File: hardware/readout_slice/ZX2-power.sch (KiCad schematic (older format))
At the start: 15 parts

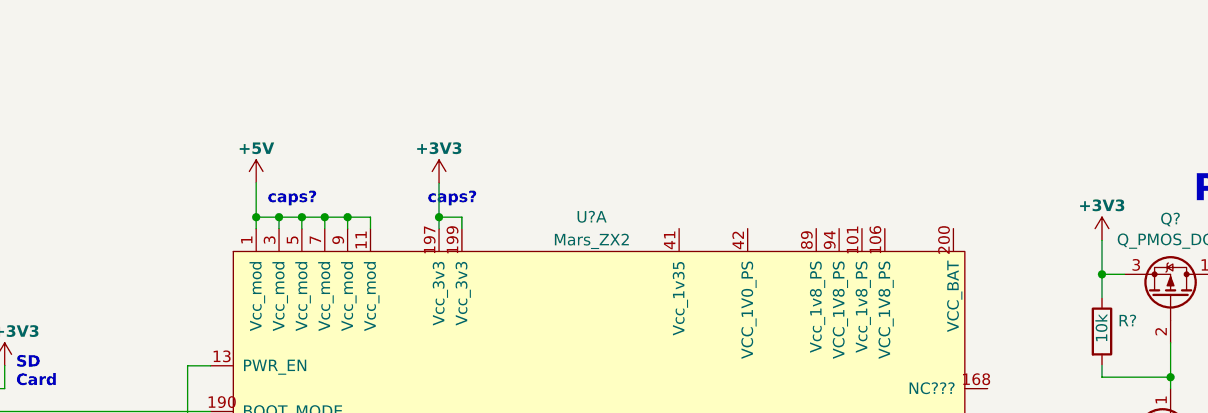
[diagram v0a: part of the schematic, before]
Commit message: more on readout_slice
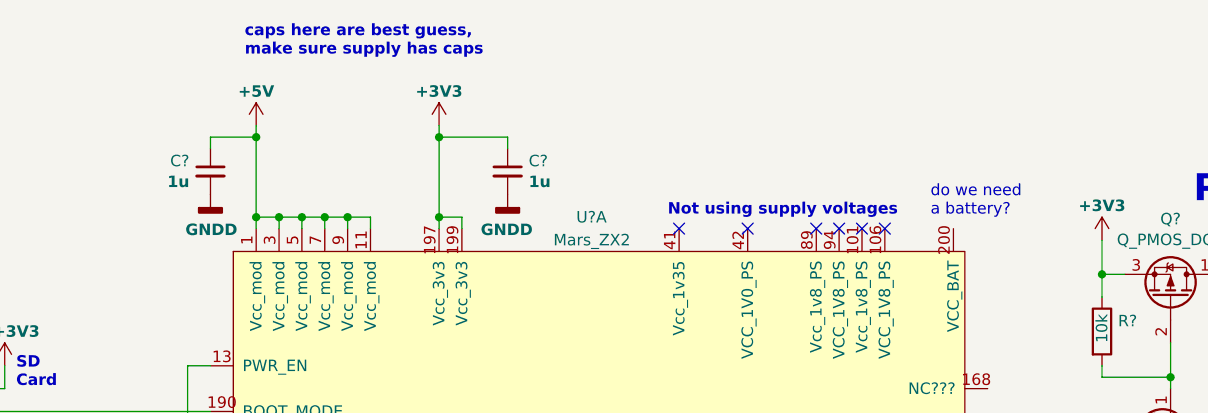
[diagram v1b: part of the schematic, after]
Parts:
- added C? (x2): 1u, symbol Device:C_Small
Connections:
- net +3V3: now also C?.1
- net +5V: now also C?.1
- net GNDD: now also C?.2, C?.2
- no-connect marks 0 -> 6
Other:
- note added: "Not using supply voltages"
- note added: "caps here are best guess,\nmake sure supply has caps"
- note added: "do we need\na battery?"
- note removed: "caps?"
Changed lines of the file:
@@
 $Descr A4 11693 8268
 encoding utf-8
-Sheet 7 10
+Sheet 5 10
 Title ""
 Date ""
@@
 Comment4 ""
 $EndDescr
-Text Notes 4350 2300 0    50   ~ 10
-caps?
-Wire Wire Line
-	4400 2350 4400 2200
+Wire Wire Line
+	4400 2350 4400 2000
 Connection ~ 4400 2350
 Wire Wire Line
@@
 	0    1    1    0
 $EndComp
-Text Notes 3650 2300 0    50   ~ 10
-caps?
 $Comp
 L power:+5V #PWR?
 U 1 1 60728782
-P 3600 2200
+P 3600 1950
 AR Path="/60728782" Ref="#PWR?"  Part="1"
 AR Path="/603D0C5A/60728782" Ref="#PWR?"  Part="1"
 AR Path="/6068976B/60728782" Ref="#PWR?"  Part="1"
 AR Path="/6086954E/608F2656/60728782" Ref="#PWR?"  Part="1"
-F 0 "#PWR?" H 3600 2050 50  0001 C CNN
-F 1 "+5V" H 3600 2350 50  0000 C CNB
-F 2 "" H 3600 2200 50  0001 C CNN
-F 3 "" H 3600 2200 50  0001 C CNN
-	1    3600 2200
+F 0 "#PWR?" H 3600 1800 50  0001 C CNN
+F 1 "+5V" H 3600 2100 50  0000 C CNB
+F 2 "" H 3600 1950 50  0001 C CNN
+F 3 "" H 3600 1950 50  0001 C CNN
+	1    3600 1950
 	1    0    0    -1
 $EndComp
@@
 L power:+3V3 #PWR?
 U 1 1 60728788
-P 4400 2200
+P 4400 1950
 AR Path="/60728788" Ref="#PWR?"  Part="1"
 AR Path="/603D0C5A/60728788" Ref="#PWR?"  Part="1"
 AR Path="/6068976B/60728788" Ref="#PWR?"  Part="1"
 AR Path="/6086954E/608F2656/60728788" Ref="#PWR?"  Part="1"
-F 0 "#PWR?" H 4400 2050 50  0001 C CNN
-F 1 "+3V3" H 4400 2350 50  0000 C CNB
-F 2 "" H 4400 2200 50  0001 C CNN
-F 3 "" H 4400 2200 50  0001 C CNN
-	1    4400 2200
+F 0 "#PWR?" H 4400 1800 50  0001 C CNN
+F 1 "+3V3" H 4400 2100 50  0000 C CNB
+F 2 "" H 4400 1950 50  0001 C CNN
+F 3 "" H 4400 1950 50  0001 C CNN
+	1    4400 1950
 	1    0    0    -1
 $EndComp
@@
 Wire Wire Line
 	3700 2400 3700 2350
-Wire Wire Line
-	3600 2350 3600 2200
 Connection ~ 3600 2350
 Wire Wire Line
@@
 Wire Notes Line width 39
 	4300 6300 4300 7850
+NoConn ~ 5450 2400
+NoConn ~ 5750 2400
+NoConn ~ 6050 2400
+NoConn ~ 6150 2400
+NoConn ~ 6250 2400
+NoConn ~ 6350 2400
+Text Notes 5400 2350 0    50   ~ 10
+Not using supply voltages
+Text Notes 6550 2350 0    50   ~ 0
+do we need\na battery?
+$Comp
+L Device:C_Small C?
+U 1 1 611B7B1F
+P 3400 2150
+F 0 "C?" H 3492 2196 50  0000 L CNN
+F 1 "1u" H 3492 2105 50  0000 L CNB
+F 2 "" H 3400 2150 50  0001 C CNN
+F 3 "~" H 3400 2150 50  0001 C CNN
+	1    3400 2150
+	-1   0    0    -1
+$EndComp
+Wire Wire Line
+	3600 2000 3400 2000
+Wire Wire Line
+	3400 2000 3400 2050
+$Comp
+L power:GNDD #PWR?
+U 1 1 611D8764
+P 3400 2250
+AR Path="/611D8764" Ref="#PWR?"  Part="1"
+AR Path="/603D0C5A/611D8764" Ref="#PWR?"  Part="1"
+AR Path="/6068976B/611D8764" Ref="#PWR?"  Part="1"
+AR Path="/6086954E/608F2656/611D8764" Ref="#PWR?"  Part="1"
+F 0 "#PWR?" H 3400 2000 50  0001 C CNN
+F 1 "GNDD" H 3404 2095 50  0000 C CNB
+F 2 "" H 3400 2250 50  0001 C CNN
+F 3 "" H 3400 2250 50  0001 C CNN
+	1    3400 2250
+	1    0    0    -1
+$EndComp
+Connection ~ 3600 2000
+Wire Wire Line
+	3600 2000 3600 1950
+Wire Wire Line
+	3600 2000 3600 2350
+$Comp
+L Device:C_Small C?
+U 1 1 611F286D
+P 4700 2150
+F 0 "C?" H 4792 2196 50  0000 L CNN
+F 1 "1u" H 4792 2105 50  0000 L CNB
+F 2 "" H 4700 2150 50  0001 C CNN
+F 3 "~" H 4700 2150 50  0001 C CNN
+	1    4700 2150
+	1    0    0    -1
+$EndComp
+Wire Wire Line
+	4700 2000 4700 2050
+$Comp
+L power:GNDD #PWR?
+U 1 1 611F2875
+P 4700 2250
+AR Path="/611F2875" Ref="#PWR?"  Part="1"
+AR Path="/603D0C5A/611F2875" Ref="#PWR?"  Part="1"
+AR Path="/6068976B/611F2875" Ref="#PWR?"  Part="1"
+AR Path="/6086954E/608F2656/611F2875" Ref="#PWR?"  Part="1"
+F 0 "#PWR?" H 4700 2000 50  0001 C CNN
+F 1 "GNDD" H 4704 2095 50  0000 C CNB
+F 2 "" H 4700 2250 50  0001 C CNN
+F 3 "" H 4700 2250 50  0001 C CNN
+	1    4700 2250
+	-1   0    0    -1
+$EndComp
+Wire Wire Line
+	4400 2000 4700 2000
+Connection ~ 4400 2000
+Wire Wire Line
+	4400 2000 4400 1950
+Text Notes 3550 1650 0    50   ~ 10
+caps here are best guess,\nmake sure supply has caps
 $EndSCHEMATC

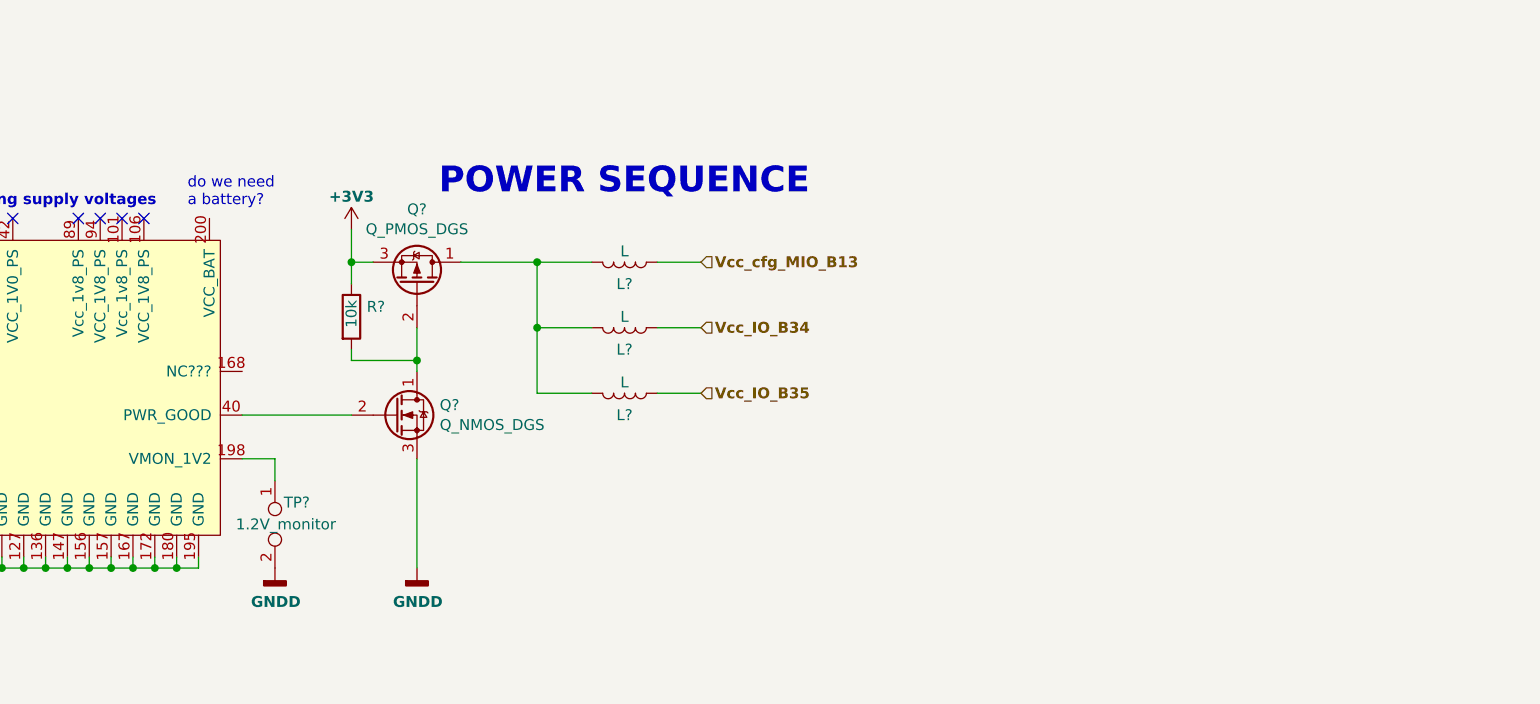
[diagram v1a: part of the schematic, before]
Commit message: added notes to schematics for readout_slice
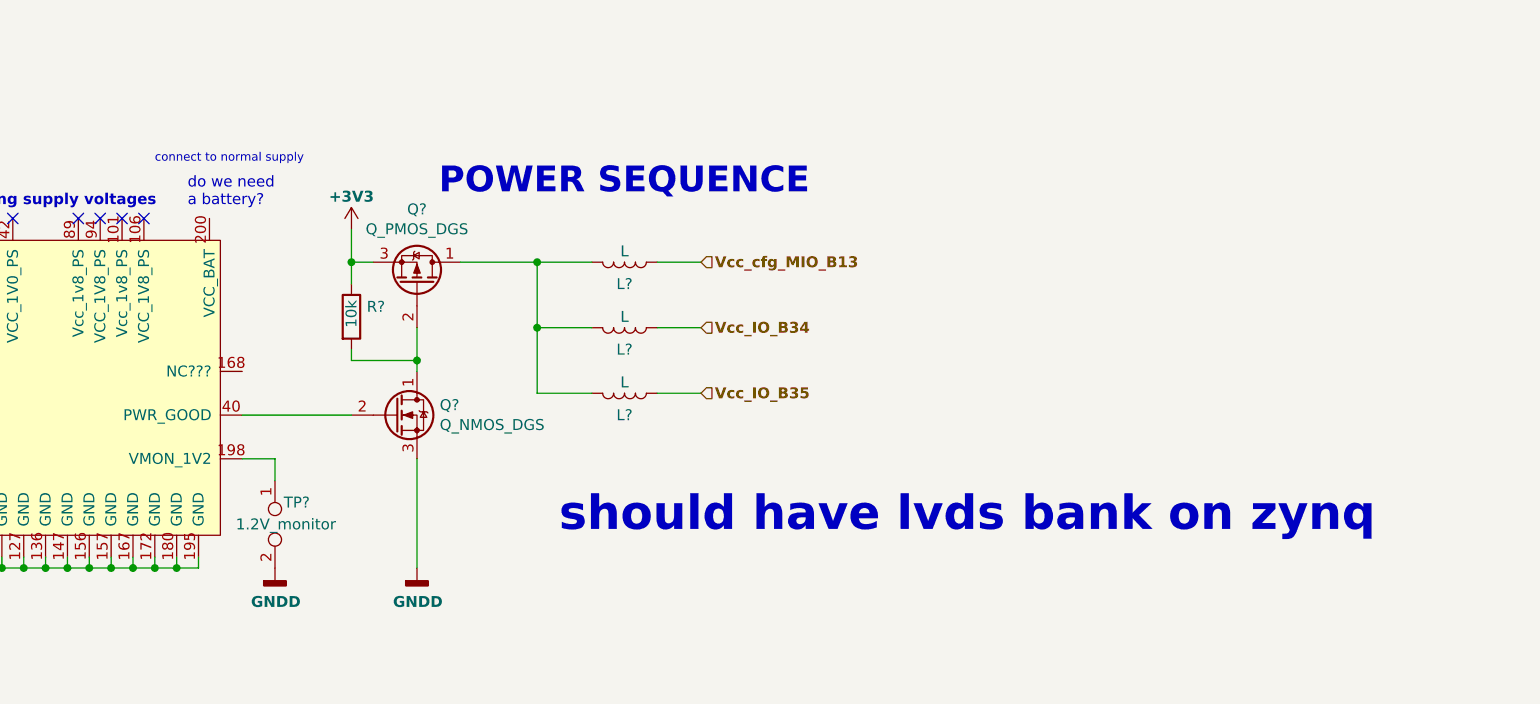
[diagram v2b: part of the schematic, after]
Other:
- note added: "connect to normal supply"
- note added: "should have lvds bank on zynq"
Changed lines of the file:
@@
 Text Notes 3550 1650 0    50   ~ 10
 caps here are best guess,\nmake sure supply has caps
+Text Notes 8250 3850 0    157  ~ 31
+should have lvds bank on zynq
+Text Notes 6400 2150 0    39   ~ 0
+connect to normal supply
 $EndSCHEMATC

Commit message: working on readout_slice
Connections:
- no-connect marks 6 -> 7
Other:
- note removed: "connect to normal supply"
- note removed: "do we need\na battery?"
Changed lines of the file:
@@
 $Descr A4 11693 8268
 encoding utf-8
-Sheet 5 10
+Sheet 14 16
 Title ""
 Date ""
@@
 	6950 3600 6950 3500
 $Comp
-L readout:Mars_ZX2 U?
-U 1 1 60728765
-P 5100 2500
-AR Path="/60728765" Ref="U?"  Part="1"
-AR Path="/603D0C5A/60728765" Ref="U?"  Part="1"
-AR Path="/6068976B/60728765" Ref="U?"  Part="1"
-AR Path="/6086954E/608F2656/60728765" Ref="U?"  Part="1"
-F 0 "U?" H 5000 2650 50  0000 L CNN
-F 1 "Mars_ZX2" H 4900 2550 50  0000 L CNN
-F 2 "" H 5150 2850 50  0001 C CNN
-F 3 "" H 5150 2850 50  0001 C CNN
-	1    5100 2500
-	1    0    0    -1
-$EndComp
-$Comp
 L Switch:SW_SPST SW?
 U 1 1 6072876B
@@
 AR Path="/6068976B/6072876B" Ref="SW?"  Part="1"
 AR Path="/6086954E/608F2656/6072876B" Ref="SW?"  Part="1"
+AR Path="/60794E14/6072876B" Ref="SW?"  Part="1"
 F 0 "SW?" V 3300 4150 50  0000 R CNN
 F 1 "SW_SPST" V 3200 4200 50  0000 R CNN
@@
 AR Path="/6068976B/60728775" Ref="#PWR?"  Part="1"
 AR Path="/6086954E/608F2656/60728775" Ref="#PWR?"  Part="1"
+AR Path="/60794E14/60728775" Ref="#PWR?"  Part="1"
 F 0 "#PWR?" H 6950 3750 50  0001 C CNN
 F 1 "GNDD" H 6954 3845 50  0000 C CNB
@@
 AR Path="/6068976B/6072877B" Ref="TP?"  Part="1"
 AR Path="/6086954E/608F2656/6072877B" Ref="TP?"  Part="1"
+AR Path="/60794E14/6072877B" Ref="TP?"  Part="1"
 F 0 "TP?" V 6850 3900 50  0000 C CNN
 F 1 "1.2V_monitor" V 6950 3850 50  0000 C CNN
@@
 AR Path="/6068976B/60728782" Ref="#PWR?"  Part="1"
 AR Path="/6086954E/608F2656/60728782" Ref="#PWR?"  Part="1"
+AR Path="/60794E14/60728782" Ref="#PWR?"  Part="1"
 F 0 "#PWR?" H 3600 1800 50  0001 C CNN
 F 1 "+5V" H 3600 2100 50  0000 C CNB
@@
 AR Path="/6068976B/60728788" Ref="#PWR?"  Part="1"
 AR Path="/6086954E/608F2656/60728788" Ref="#PWR?"  Part="1"
+AR Path="/60794E14/60728788" Ref="#PWR?"  Part="1"
 F 0 "#PWR?" H 4400 1800 50  0001 C CNN
 F 1 "+3V3" H 4400 2100 50  0000 C CNB
@@
 AR Path="/6068976B/6072879F" Ref="J?"  Part="1"
 AR Path="/6086954E/608F2656/6072879F" Ref="J?"  Part="1"
+AR Path="/60794E14/6072879F" Ref="J?"  Part="1"
 F 0 "J?" H 2118 3517 50  0000 C CNN
 F 1 "3 pin Jumper" H 2250 3400 50  0000 C CNN
@@
 AR Path="/6068976B/607287A7" Ref="#PWR?"  Part="1"
 AR Path="/6086954E/608F2656/607287A7" Ref="#PWR?"  Part="1"
+AR Path="/60794E14/607287A7" Ref="#PWR?"  Part="1"
 F 0 "#PWR?" H 2500 2850 50  0001 C CNN
 F 1 "+3V3" H 2550 3150 50  0000 C CNB
@@
 AR Path="/6068976B/607287B4" Ref="#PWR?"  Part="1"
 AR Path="/6086954E/608F2656/607287B4" Ref="#PWR?"  Part="1"
+AR Path="/60794E14/607287B4" Ref="#PWR?"  Part="1"
 F 0 "#PWR?" H 3600 3900 50  0001 C CNN
 F 1 "GNDD" H 3604 3995 50  0000 C CNB
@@
 AR Path="/6068976B/607287BA" Ref="#PWR?"  Part="1"
 AR Path="/6086954E/608F2656/607287BA" Ref="#PWR?"  Part="1"
+AR Path="/60794E14/607287BA" Ref="#PWR?"  Part="1"
 F 0 "#PWR?" H 3300 3900 50  0001 C CNN
 F 1 "GNDD" H 3304 3995 50  0000 C CNB
@@
 AR Path="/6068976B/607287C0" Ref="#PWR?"  Part="1"
 AR Path="/6086954E/608F2656/607287C0" Ref="#PWR?"  Part="1"
+AR Path="/60794E14/607287C0" Ref="#PWR?"  Part="1"
 F 0 "#PWR?" H 2500 3150 50  0001 C CNN
 F 1 "GNDD" H 2504 3245 50  0000 C CNB
@@
 AR Path="/6068976B/607287C8" Ref="Q?"  Part="1"
 AR Path="/6086954E/608F2656/607287C8" Ref="Q?"  Part="1"
+AR Path="/60794E14/607287C8" Ref="Q?"  Part="1"
 F 0 "Q?" V 7942 2700 50  0000 C CNN
 F 1 "Q_PMOS_DGS" V 7851 2700 50  0000 C CNN
@@
 AR Path="/6068976B/607287CE" Ref="Q?"  Part="1"
 AR Path="/6086954E/608F2656/607287CE" Ref="Q?"  Part="1"
+AR Path="/60794E14/607287CE" Ref="Q?"  Part="1"
 F 0 "Q?" H 7704 3346 50  0000 L CNN
 F 1 "Q_NMOS_DGS" H 7704 3255 50  0000 L CNN
@@
 AR Path="/6068976B/607287D5" Ref="#PWR?"  Part="1"
 AR Path="/6086954E/608F2656/607287D5" Ref="#PWR?"  Part="1"
+AR Path="/60794E14/607287D5" Ref="#PWR?"  Part="1"
 F 0 "#PWR?" H 7600 3750 50  0001 C CNN
 F 1 "GNDD" H 7604 3845 50  0000 C CNB
@@
 AR Path="/6068976B/607287DC" Ref="R?"  Part="1"
 AR Path="/6086954E/608F2656/607287DC" Ref="R?"  Part="1"
+AR Path="/60794E14/607287DC" Ref="R?"  Part="1"
 F 0 "R?" H 7370 2896 50  0000 L CNN
 F 1 "10k" V 7300 2800 50  0000 L CNN
@@
 AR Path="/6068976B/607287EB" Ref="#PWR?"  Part="1"
 AR Path="/6086954E/608F2656/607287EB" Ref="#PWR?"  Part="1"
+AR Path="/60794E14/607287EB" Ref="#PWR?"  Part="1"
 F 0 "#PWR?" H 7300 2300 50  0001 C CNN
 F 1 "+3V3" H 7300 2600 50  0000 C CNB
@@
 AR Path="/6068976B/607287F1" Ref="L?"  Part="1"
 AR Path="/6086954E/608F2656/607287F1" Ref="L?"  Part="1"
+AR Path="/60794E14/607287F1" Ref="L?"  Part="1"
 F 0 "L?" V 8650 2600 50  0000 C CNN
 F 1 "L" V 8500 2600 50  0000 C CNN
@@
 AR Path="/6068976B/607287F7" Ref="L?"  Part="1"
 AR Path="/6086954E/608F2656/607287F7" Ref="L?"  Part="1"
+AR Path="/60794E14/607287F7" Ref="L?"  Part="1"
 F 0 "L?" V 8650 2900 50  0000 C CNN
 F 1 "L" V 8500 2900 50  0000 C CNN
@@
 AR Path="/6068976B/607287FD" Ref="L?"  Part="1"
 AR Path="/6086954E/608F2656/607287FD" Ref="L?"  Part="1"
+AR Path="/60794E14/607287FD" Ref="L?"  Part="1"
 F 0 "L?" V 8650 3200 50  0000 C CNN
 F 1 "L" V 8500 3200 50  0000 C CNN
@@
 AR Path="/6068976B/60792C9E" Ref="U?"  Part="1"
 AR Path="/6086954E/608F2656/60792C9E" Ref="U?"  Part="1"
+AR Path="/60794E14/60792C9E" Ref="U?"  Part="1"
 F 0 "U?" H 3050 7000 50  0000 C CNB
 F 1 "BS3" H 3050 6800 50  0000 C CNB
@@
 AR Path="/6068976B/60792CA4" Ref="C?"  Part="1"
 AR Path="/6086954E/608F2656/60792CA4" Ref="C?"  Part="1"
+AR Path="/60794E14/60792CA4" Ref="C?"  Part="1"
 F 0 "C?" H 1308 7446 50  0000 R CNB
 F 1 "10n" H 1308 7355 50  0000 R CNB
@@
 AR Path="/6068976B/60792CAA" Ref="#PWR?"  Part="1"
 AR Path="/6086954E/608F2656/60792CAA" Ref="#PWR?"  Part="1"
+AR Path="/60794E14/60792CAA" Ref="#PWR?"  Part="1"
 F 0 "#PWR?" H 1400 7250 50  0001 C CNN
 F 1 "GNDD" H 1404 7345 50  0000 C CNB
@@
 AR Path="/6068976B/60792CB0" Ref="C?"  Part="1"
 AR Path="/6086954E/608F2656/60792CB0" Ref="C?"  Part="1"
+AR Path="/60794E14/60792CB0" Ref="C?"  Part="1"
 F 0 "C?" H 2558 7446 50  0000 R CNB
 F 1 "10n" H 2558 7355 50  0000 R CNB
@@
 AR Path="/6068976B/60792CCC" Ref="R?"  Part="1"
 AR Path="/6086954E/608F2656/60792CCC" Ref="R?"  Part="1"
+AR Path="/60794E14/60792CCC" Ref="R?"  Part="1"
 F 0 "R?" H 1470 6946 50  0000 L CNN
 F 1 "10k" V 1400 6850 50  0000 L CNN
@@
 AR Path="/6068976B/60792CD4" Ref="#PWR?"  Part="1"
 AR Path="/6086954E/608F2656/60792CD4" Ref="#PWR?"  Part="1"
+AR Path="/60794E14/60792CD4" Ref="#PWR?"  Part="1"
 F 0 "#PWR?" H 1400 6600 50  0001 C CNN
 F 1 "+3V3" H 1400 6900 50  0000 C CNB
@@
 AR Path="/6068976B/60792CE0" Ref="#PWR?"  Part="1"
 AR Path="/6086954E/608F2656/60792CE0" Ref="#PWR?"  Part="1"
+AR Path="/60794E14/60792CE0" Ref="#PWR?"  Part="1"
 F 0 "#PWR?" H 2050 7250 50  0001 C CNN
 F 1 "GNDD" H 2054 7345 50  0000 C CNB
@@
 AR Path="/6068976B/60792CE6" Ref="#PWR?"  Part="1"
 AR Path="/6086954E/608F2656/60792CE6" Ref="#PWR?"  Part="1"
+AR Path="/60794E14/60792CE6" Ref="#PWR?"  Part="1"
 F 0 "#PWR?" H 2650 7250 50  0001 C CNN
 F 1 "GNDD" H 2654 7345 50  0000 C CNB
@@
 AR Path="/6068976B/60792CEC" Ref="#PWR?"  Part="1"
 AR Path="/6086954E/608F2656/60792CEC" Ref="#PWR?"  Part="1"
+AR Path="/60794E14/60792CEC" Ref="#PWR?"  Part="1"
 F 0 "#PWR?" H 3300 7250 50  0001 C CNN
 F 1 "GNDD" H 3304 7345 50  0000 C CNB
@@
 AR Path="/6068976B/60792CF2" Ref="U?"  Part="1"
 AR Path="/6086954E/608F2656/60792CF2" Ref="U?"  Part="1"
+AR Path="/60794E14/60792CF2" Ref="U?"  Part="1"
 F 0 "U?" H 1800 7000 50  0000 C CNB
 F 1 "BS3" H 1800 6800 50  0000 C CNB
@@
 NoConn ~ 6250 2400
 NoConn ~ 6350 2400
-Text Notes 5400 2350 0    50   ~ 10
+Text Notes 5550 2300 0    50   ~ 10
 Not using supply voltages
-Text Notes 6550 2350 0    50   ~ 0
-do we need\na battery?
 $Comp
 L Device:C_Small C?
@@
 AR Path="/6068976B/611D8764" Ref="#PWR?"  Part="1"
 AR Path="/6086954E/608F2656/611D8764" Ref="#PWR?"  Part="1"
+AR Path="/60794E14/611D8764" Ref="#PWR?"  Part="1"
 F 0 "#PWR?" H 3400 2000 50  0001 C CNN
 F 1 "GNDD" H 3404 2095 50  0000 C CNB
@@
 AR Path="/6068976B/611F2875" Ref="#PWR?"  Part="1"
 AR Path="/6086954E/608F2656/611F2875" Ref="#PWR?"  Part="1"
+AR Path="/60794E14/611F2875" Ref="#PWR?"  Part="1"
 F 0 "#PWR?" H 4700 2000 50  0001 C CNN
 F 1 "GNDD" H 4704 2095 50  0000 C CNB
@@
 Text Notes 8250 3850 0    157  ~ 31
 should have lvds bank on zynq
-Text Notes 6400 2150 0    39   ~ 0
-connect to normal supply
+NoConn ~ 6650 2400
+$Comp
+L readout:Mars_ZX2 U?
+U 1 1 60728765
+P 5100 2500
+AR Path="/60728765" Ref="U?"  Part="1"
+AR Path="/603D0C5A/60728765" Ref="U?"  Part="1"
+AR Path="/6068976B/60728765" Ref="U?"  Part="1"
+AR Path="/6086954E/608F2656/60728765" Ref="U?"  Part="1"
+AR Path="/60794E14/60728765" Ref="U?"  Part="1"
+F 0 "U?" H 5000 2650 50  0000 L CNN
+F 1 "Mars_ZX2" H 4900 2550 50  0000 L CNN
+F 2 "" H 5150 2850 50  0001 C CNN
+F 3 "" H 5150 2850 50  0001 C CNN
+	1    5100 2500
+	1    0    0    -1
+$EndComp
 $EndSCHEMATC
